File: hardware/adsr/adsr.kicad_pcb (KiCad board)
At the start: 4 copper layers, 29 x 100 mm, 61 parts, among them J1 MonoJack, J2 MonoJack, J4 Conn_02x05_Odd_Even, Q1 BC847, Q2 BC847, Q3 BC847, Q4 BC847, Q5 BC847, Q6 2N7002K, SW1 SW_DPDT_x2, SW2 SW_Push, U1 ICM7556, U2 TL074

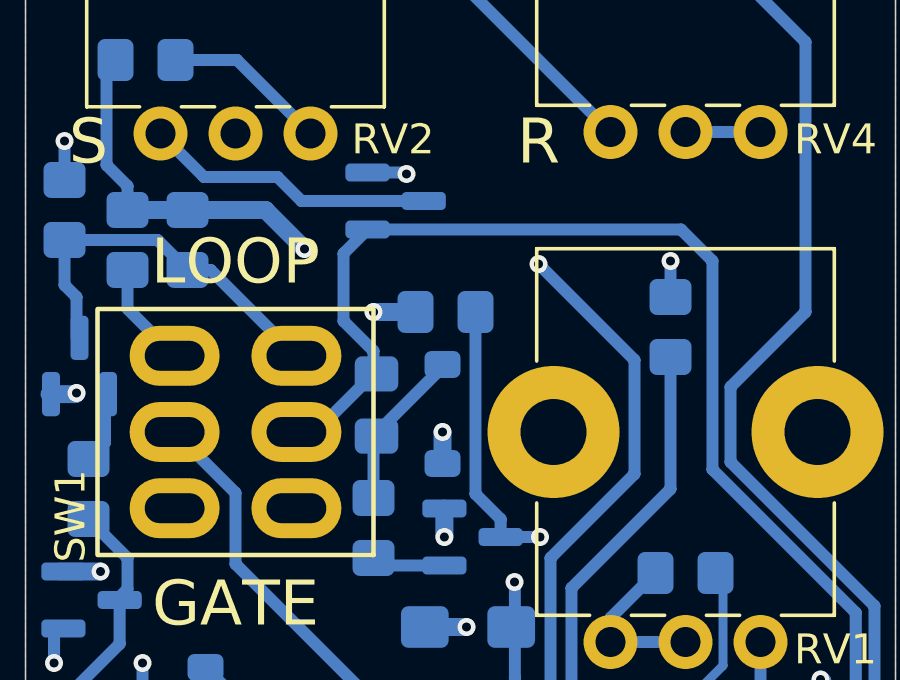
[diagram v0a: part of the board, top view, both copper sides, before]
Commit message: Added missing gate R on MOSFET
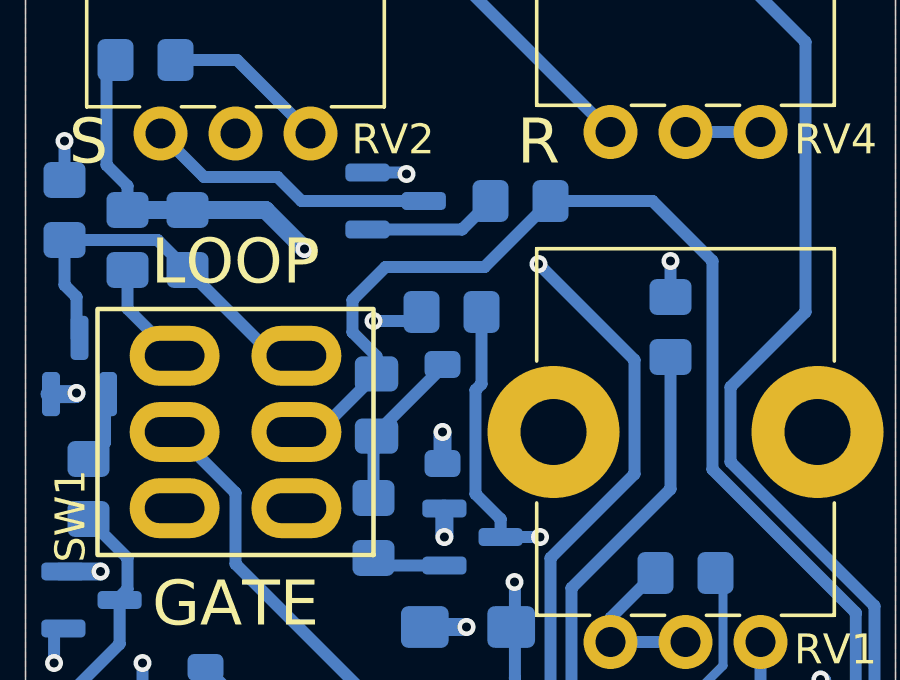
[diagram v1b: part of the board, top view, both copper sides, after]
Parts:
- added R17: 1M, Resistor_SMD:R_0805_2012Metric_Pad1.20x1.40mm_HandSolder, B.Cu at (116.5, 82.3)
- moved R12 0.20 mm to (114.2, 86.0)
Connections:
- C3 pad 2: Net-(Q6-G) -> Net-(SW1A-B)
- SW1 pad 2: Net-(Q6-G) -> Net-(SW1A-B)
- U1 pad 4: Net-(Q6-G) -> Net-(SW1A-B)
- U2 pad 12: Net-(Q6-G) -> Net-(SW1A-B)
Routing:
- net Net-(SW1A-B): track 0.00 -> 59.5 mm, vias 0 -> 1
- net Net-(Q6-G): track 59.9 -> 4.49 mm, vias 1 -> 0

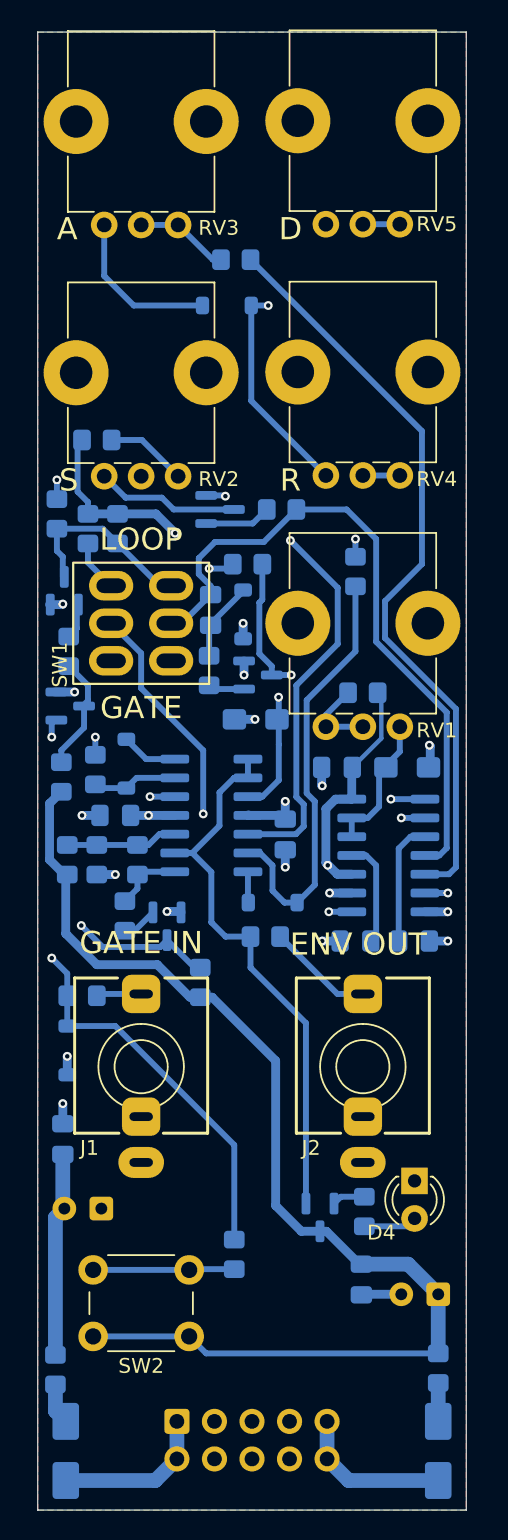
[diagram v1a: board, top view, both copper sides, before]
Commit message: added mechanical hole and final silk cleanup
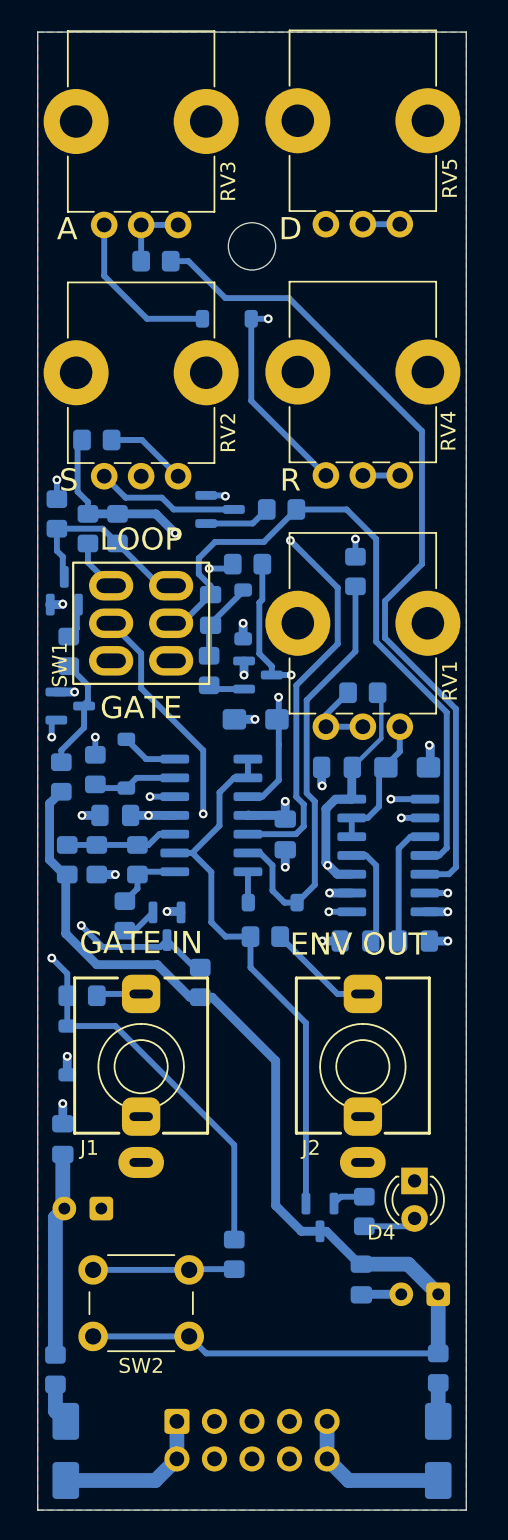
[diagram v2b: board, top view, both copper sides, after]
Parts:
- added H1: MountingHole, MountingHole:MountingHole_3.2mm_M3_DIN965, F.Cu at (114.5, 64.5)
- moved R14 5.40 mm to (108.0, 65.5)
- moved D1 0.90 mm to (112.8, 69.4)
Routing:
- net Net-(U1A-Q): track 51.2 -> 56.6 mm
- net Net-(R14-Pad2): track 6.37 -> 4.95 mm
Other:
- board text added: "Thank yous: Rene Schmitz, Moritz Klein, Yves Usson, Eddy Bergman, Kassutronics"
- board text removed: "GATE BUTTON TO TN ON GATE IN"
- board text removed: "Thank yous: Rene Schmitz, Moritz Klein, Yves Usson, Eddy Bergman, Kausstronics"
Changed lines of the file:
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@@
 			(plot_on_all_layers_selection 0x00000000_00000000_00000000_00000000)
 			(disableapertmacros no)
-			(usegerberextensions no)
+			(usegerberextensions yes)
 			(usegerberattributes yes)
 			(usegerberadvancedattributes yes)
-			(creategerberjobfile yes)
+			(creategerberjobfile no)
 			(dashed_line_dash_ratio 12.000000)
 			(dashed_line_gap_ratio 3.000000)
@@
 			(plotpadnumbers no)
 			(hidednponfab no)
-			(sketchdnponfab yes)
-			(crossoutdnponfab yes)
-			(subtractmaskfromsilk no)
+			(sketchdnponfab no)
+			(crossoutdnponfab no)
+			(subtractmaskfromsilk yes)
 			(outputformat 1)
 			(mirror no)
-			(drillshape 1)
+			(drillshape 0)
 			(scaleselection 1)
-			(outputdirectory "")
+			(outputdirectory "../plots/adsr/")
 		)
 	)
@@
 		(tags "Potentiometer vertical Bourns PTV09A-1 Single")
 		(property "Reference" "RV5"
-			(at 0 2.5 0)
+			(at 3.1 3.4 90)
 			(layer "F.SilkS")
 			(effects
@@
 		(tags "Potentiometer vertical Bourns PTV09A-1 Single")
 		(property "Reference" "RV3"
-			(at -0.2 2.75 0)
+			(at 2.95 3.4 90)
 			(layer "F.SilkS")
 			(effects
@@
 		(tags "Potentiometer vertical Bourns PTV09A-1 Single")
 		(property "Reference" "RV4"
-			(at -0.25 2.5 180)
+			(at 3 3.3 270)
 			(layer "F.SilkS")
 			(effects
@@
 		)
 	)
+	(footprint "MountingHole:MountingHole_3.2mm_M3_DIN965"
+		(layer "F.Cu")
+		(at 114.5 64.5)
+		(descr "Mounting Hole 3.2mm, M3, no annular, generated by kicad-footprint-generator mountinghole.py")
+		(tags "mountinghole M3 DIN965")
+		(property "Reference" "H1"
+			(at 0 -3.75 0)
+			(layer "F.SilkS")
+			(hide yes)
+			(effects
+				(font
+					(size 1 1)
+					(thickness 0.15)
+				)
+			)
+		)
+		(property "Value" "MountingHole"
+			(at 0 3.75 0)
+			(layer "F.Fab")
+			(effects
+				(font
+					(size 1 1)
+					(thickness 0.15)
+				)
+			)
+		)
+		(property "Datasheet" ""
+			(at 0 0 0)
+			(layer "F.Fab")
+			(hide yes)
+			(effects
+				(font
+					(size 1.27 1.27)
+					(thickness 0.15)
+				)
+			)
+		)
+		(property "Description" "Mounting Hole without connection"
+			(at 0 0 0)
+			(layer "F.Fab")
+			(hide yes)
+			(effects
+				(font
+					(size 1.27 1.27)
+					(thickness 0.15)
+				)
+			)
+		)
+		(property ki_fp_filters "MountingHole*")
+		(sheetname "/")
+		(sheetfile "adsr.kicad_sch")
+		(attr exclude_from_pos_files exclude_from_bom)
+		(fp_circle
+			(center 0 0)
+			(end 2.8 0)
+			(stroke
+				(width 0.15)
+				(type solid)
+			)
+			(fill no)
+			(layer "Cmts.User")
+		)
+		(fp_circle
+			(center 0 0)
+			(end 3.05 0)
+			(stroke
+				(width 0.05)
+				(type solid)
+			)
+			(fill no)
+			(layer "F.CrtYd")
+		)
+		(fp_text user "${REFERENCE}"
+			(at 0 0 0)
+			(layer "F.Fab")
+			(effects
+				(font
+					(size 1 1)
+					(thickness 0.15)
+				)
+			)
+		)
+		(pad "" np_thru_hole circle
+			(at 0 0)
+			(size 3.2 3.2)
+			(drill 3.2)
+			(layers "*.Cu" "*.Mask")
+		)
+		(embedded_fonts no)
+	)
 	(footprint "LED_THT:LED_D3.0mm"
 		(layer "F.Cu")
@@
 		(tags "Potentiometer vertical Bourns PTV09A-1 Single")
 		(property "Reference" "RV1"
-			(at -0.25 2.5 180)
+			(at 3.1 3.4 270)
 			(layer "F.SilkS")
 			(effects
@@
 		(tags "Potentiometer vertical Bourns PTV09A-1 Single")
 		(property "Reference" "RV2"
-			(at -0.2 2.75 180)
+			(at 2.95 3.4 270)
 			(layer "F.SilkS")
 			(effects
@@
 	(footprint "Resistor_SMD:R_0805_2012Metric_Pad1.20x1.40mm_HandSolder"
 		(layer "B.Cu")
-		(at 113.4 65.4 180)
+		(at 108 65.5 180)
 		(descr "Resistor SMD 0805 (2012 Metric), square (rectangular) end terminal, IPC-7351 nominal with elongated pad for handsoldering. (Body size source: IPC-SM-782 page 72, https://www.pcb-3d.com/wordpress/wp-content/uploads/ipc-sm-782a_amendment_1_and_2.pdf), generated with kicad-footprint-generator")
 		(tags "resistor handsolder")
@@
 	(footprint "Diode_SMD:D_SOD-123"
 		(layer "B.Cu")
-		(at 112.8 68.5 180)
+		(at 112.8 69.4 180)
 		(descr "SOD-123")
 		(tags "SOD-123")
@@
 		(layer "Cmts.User")
 	)
-	(gr_line
-		(start 147.8 106.3)
-		(end 224.8 106.3)
-		(stroke
-			(width 0.1)
-			(type default)
-		)
-		(layer "Cmts.User")
-	)
 	(gr_rect
 		(start 100 50)
@@
 		)
 	)
-	(gr_text "Thank yous: Rene Schmitz, Moritz Klein, \nYves Usson, Eddy Bergman, Kausstronics"
+	(gr_text "Thank yous: Rene Schmitz, Moritz Klein, \nYves Usson, Eddy Bergman, Kassutronics"
 		(at 128.6 61.6 0)
 		(layer "B.SilkS")
@@
 		)
 	)
-	(gr_text "GATE BUTTON TO TN ON GATE IN"
-		(at 150.6 108.5 0)
-		(layer "Cmts.User")
-		(effects
-			(font
-				(size 3 3)
-				(thickness 0.4)
-			)
-			(justify left bottom)
-		)
-	)
 	(gr_text "CHECK POT ORIENTATIONS"
 		(at 162.2 97.4 0)
@@
 		(layer "Cmts.User")
 		(pts
+			(xy 114.5 64.5) (xy 122 56)
+		)
+		(height 16.3)
+		(orientation 1)
+		(format
+			(prefix "")
+			(suffix "")
+			(units 3)
+			(units_format 1)
+			(precision 4)
+		)
+		(style
+			(thickness 0.1)
+			(arrow_length 1.27)
+			(text_position_mode 0)
+			(arrow_direction outward)
+			(extension_height 0.58642)
+			(extension_offset 0.5)
+			(keep_text_aligned yes)
+		)
+		(gr_text "8.5000 mm"
+			(at 129.65 60.25 90)
+			(layer "Cmts.User")
+			(effects
+				(font
+					(size 1 1)
+					(thickness 0.15)
+				)
+			)
+		)
+	)
+	(dimension
+		(type orthogonal)
+		(layer "Cmts.User")
+		(pts
 			(xy 107 56.05) (xy 122 56)
 		)
@@
 	)
 	(via
-		(at 115.6 68.5)
+		(at 115.6 69.4)
 		(size 0.6)
 		(drill 0.3)
@@
 	)
 	(segment
-		(start 114.45 68.5)
-		(end 115.6 68.5)
+		(start 115.199999 101.73)
+		(end 114.225 101.73)
 		(width 0.4)
 		(layer "B.Cu")
@@
 	)
 	(segment
-		(start 114.45 74.95)
-		(end 114.45 68.6)
+		(start 114.45 69.4)
+		(end 114.45 74.95)
 		(width 0.4)
 		(layer "B.Cu")
@@
 	)
 	(segment
-		(start 115.199999 101.73)
-		(end 114.225 101.73)
+		(start 119.4 80.1)
+		(end 119.5 80)
 		(width 0.4)
 		(layer "B.Cu")
@@
 	)
 	(segment
-		(start 119.4 80.1)
-		(end 119.5 80)
+		(start 116.3125 95.0125)
+		(end 116.3 95)
 		(width 0.4)
 		(layer "B.Cu")
@@
 	)
 	(segment
-		(start 116.3125 95.0125)
-		(end 116.3 95)
+		(start 114.45 69.4)
+		(end 115.6 69.4)
 		(width 0.4)
 		(layer "B.Cu")
@@
 	)
 	(segment
-		(start 114.45 68.6)
-		(end 114.45 68.5)
+		(start 119.5 65.5)
+		(end 119.5 63)
 		(width 0.4)
-		(layer "B.Cu")
+		(layer "In1.Cu")
 		(net 6)
 	)
@@
 	)
 	(segment
-		(start 119.5 63)
-		(end 119.5 64.6)
-		(width 0.4)
-		(layer "In1.Cu")
-		(net 6)
-	)
-	(segment
-		(start 119.5 64.6)
-		(end 115.6 68.5)
+		(start 115.6 69.4)
+		(end 119.5 65.5)
 		(width 0.4)
 		(layer "In1.Cu")
@@
 	)
 	(segment
-		(start 104.5 66.5)
-		(end 104.5 63.05)
+		(start 111.15 69.4)
+		(end 107.4 69.4)
 		(width 0.4)
 		(layer "B.Cu")
@@
 	)
 	(segment
-		(start 111.15 68.5)
-		(end 106.5 68.5)
+		(start 107.4 69.4)
+		(end 104.5 66.5)
 		(width 0.4)
 		(layer "B.Cu")
@@
 	)
 	(segment
-		(start 106.5 68.5)
-		(end 104.5 66.5)
+		(start 104.5 66.5)
+		(end 104.5 63.05)
 		(width 0.4)
 		(layer "B.Cu")
@@
 	)
 	(segment
-		(start 123.5 91)
-		(end 128.299 95.799)
+		(start 126 77)
+		(end 126 86)
+		(width 0.4)
+		(layer "B.Cu")
+		(net 33)
+	)
+	(segment
+		(start 123.5 88.5)
+		(end 123.5 91)
 		(width 0.4)
 		(layer "B.Cu")
@@
 	)
 	(segment
-		(start 114.4 65.4)
+		(start 117 68)
 		(end 126 77)
 		(width 0.4)
@@
 	)
 	(segment
-		(start 126 77)
-		(end 126 86)
+		(start 123.5 91)
+		(end 128.299 95.799)
+		(width 0.4)
+		(layer "B.Cu")
+		(net 33)
+	)
+	(segment
+		(start 126 86)
+		(end 123.5 88.5)
 		(width 0.4)
 		(layer "B.Cu")
@@
 	)
 	(segment
-		(start 126 86)
-		(end 123.5 88.5)
+		(start 112.7 68)
+		(end 117 68)
 		(width 0.4)
 		(layer "B.Cu")
@@
 	)
 	(segment
-		(start 127.828275 106.98)
-		(end 126.2 106.98)
+		(start 109 65.5)
+		(end 110.2 65.5)
 		(width 0.4)
 		(layer "B.Cu")
@@
 	)
 	(segment
-		(start 123.5 88.5)
-		(end 123.5 91)
+		(start 127.828275 106.98)
+		(end 126.2 106.98)
 		(width 0.4)
 		(layer "B.Cu")
@@
 	)
 	(segment
-		(start 111.85 65.4)
-		(end 109.5 63.05)
+		(start 110.2 65.5)
+		(end 112.7 68)
 		(width 0.4)
 		(layer "B.Cu")
-		(net 34)
+		(net 33)
 	)
 	(segment
@@
 	)
 	(segment
-		(start 112.4 65.4)
-		(end 111.85 65.4)
+		(start 107 65.5)
+		(end 107 63.05)
 		(width 0.4)
 		(layer "B.Cu")
